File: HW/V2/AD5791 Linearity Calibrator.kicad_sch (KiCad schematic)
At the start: 13 parts, among them J7 Conn_01x32, U1 7533, U2 L78L15, U3 L79L15

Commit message: v2
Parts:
- removed J5, J6: ~, 100mm template footprints:CTB93HD3, symbol Connector_Generic:Conn_01x03
- added C1: 10pF, Resistor_SMD:R_0603_1608Metric, symbol Device:C_Small
- added C1, C3, C4: 10uF, Resistor_SMD:R_0603_1608Metric, symbol Device:C_Small
- added C10, C11, C12, C13, C14, C4, C9: 100nF, Capacitor_SMD:C_0603_1608Metric, symbol Device:C_Small
- added D1, D4: 5819, Resistor_SMD:R_0603_1608Metric_Pad0.98x0.95mm_HandSolder, symbol Device:D_Small
- added H1, H2: MountingHole_Pad, MountingHole:MountingHole_3.2mm_M3_Pad_Via, symbol Mechanical:MountingHole_Pad
- added R1, R2, R3, R4, R5, R6, R7: 10R, Resistor_SMD:R_0603_1608Metric, symbol Device:R
- added SW1: RST, Button_Switch_SMD:SW_SPST_B3U-1000P, symbol Switch:SW_SPST
- added U2: AD5791BRUZ, AD5791BRUZ:SOP65P640X120-20N, symbol AD5791BRUZ:AD5791BRUZ
- added U4: LT1021, Package_DIP:DIP-8_W7.62mm, symbol Reference_Voltage:LT1019xN8
- added U6: +BUFF, Package_SO:SOIC-8_3.9x4.9mm_P1.27mm, symbol Better Op-Amp:Better_Op-Amp
- added U7: -BUFF, Package_SO:SOIC-8_3.9x4.9mm_P1.27mm, symbol Better Op-Amp:Better_Op-Amp
- added U8: Pico, MCU_RaspberryPi_and_Boards:RPi_Pico_SMD_TH, symbol MCU_RaspberryPi_and_Boards:Pico
- added U9: OBUFF, Package_SO:SOIC-8_3.9x4.9mm_P1.27mm, symbol Better Op-Amp:Better_Op-Amp
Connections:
- net GND: now also J1.2 (Pin_2), C1.2, C10.1, C11.1, C12.1, C13.1, C14.1, C3.2, C4.1, C4.2, C9.1, H1.1, H2.1, SW1.1 (A), U2.15 (DGND), U4.4 (GND), U7.3 (+), U8.13 (GND), U8.18 (GND), U8.23 (GND), U8.28 (GND), U8.3 (GND), U8.33 (AGND), U8.37 (3V3_EN), U8.38 (GND), U8.42 (GND), U8.8 (GND)
- net +3.3V: now reaches C1.1, U1.3 (VOUT)
- net +3.3V: now also C3.1, D4.2 (A), U2.10 (IOVCC), U2.9 (VCC), U8.36 (3V3)
- net at U3.2 (VI): now also J1.1 (Pin_1)
- net -15V: now reaches C3.2, U3.3 (VO)
- net -15V: now also C4.1, R5.1, R6.1, R7.1, U2.18 (VSS)
- net +15V: now reaches C2.1, U1.2 (VIN), U2.1 (OUT)
- net +15V: now also C1.1, D4.1 (K), R1.1, R2.1, R3.1, R4.1, U2.5 (VDD)
- net at U2.3 (IN): now also J1.3 (Pin_3)
- new net: C9.2, R2.2, U6.7 (V+)
- new net: C13.2, R6.2, U7.4 (V-)
- new net: SW1.2 (B), U8.30 (RUN)
- new net: C10.2, R3.2, U7.7 (V+)
- new net: C14.2, R7.2, U9.4 (V-)
- new net: C11.2, R4.2, U9.7 (V+)
- new net: C4.2, R1.2, U4.2 (IN)
- new net: C1.1, U2.20 (RFB), U9.6
- new net: C1.2, U2.1 (INV), U9.2 (-)
- new net: C12.2, R5.2, U6.4 (V-)
- new net: D1.2 (A), U8.39 (VSYS)
- new net: U2.2 (VOUT), U9.3 (+)
- new net 10VREF: U4.6 (OUT), U6.3 (+)
- new net 3V3IN: D1.1 (K)
- new net ALERT: U8.21 (GPIO16)
- new net GNDA: U2.19 (AGND)
- new net SCLK: U2.13 (SCLK), U8.7 (GPIO5)
- new net SDIN: U2.12 (SDIN), U8.6 (GPIO4)
- new net SDO: U2.11 (SDO), U8.5 (GPIO3)
- new net UART_RX: U8.2 (GPIO1)
- new net UART_TX: U8.1 (GPIO0)
- new net VREFNF: U2.16 (VREFNF), U7.6
- new net VREFNS: U2.17 (VREFNS), U7.2 (-)
- new net VREFPF: U2.4 (VREFPF), U6.6
- new net VREFPS: U2.3 (VREFPS), U6.2 (-)
- new net ~{CLR}: U2.7 (~{CLR}), U8.11 (GPIO8)
- new net ~{LDAC}: U2.8 (~{LDAC}), U8.12 (GPIO9)
- new net ~{RESET}: U2.6 (~{RESET}), U8.10 (GPIO7)
- new net ~{SYNC}: U2.14 (~{SYNC}), U8.9 (GPIO6)
- no-connect marks 0 -> 9
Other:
- note added: "On-board 3V3 reg deactivated"
- moved on the sheet: J1, J2, J3, J4, J7

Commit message: finalized schematics for v2
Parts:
- removed C1: 10pF, Resistor_SMD:R_0603_1608Metric, symbol Device:C_Small
- removed C4: 100nF, Capacitor_SMD:C_0603_1608Metric, symbol Device:C_Small
- removed D1: 5819, Resistor_SMD:R_0603_1608Metric_Pad0.98x0.95mm_HandSolder, symbol Device:D_Small
- removed R1: 10R, Resistor_SMD:R_0603_1608Metric, symbol Device:R
- removed U4: LT1021, Package_DIP:DIP-8_W7.62mm, symbol Reference_Voltage:LT1019xN8
- removed U6: +BUFF, Package_SO:SOIC-8_3.9x4.9mm_P1.27mm, symbol Better Op-Amp:Better_Op-Amp
- removed U7: -BUFF, Package_SO:SOIC-8_3.9x4.9mm_P1.27mm, symbol Better Op-Amp:Better_Op-Amp
- removed U9: OBUFF, Package_SO:SOIC-8_3.9x4.9mm_P1.27mm, symbol Better Op-Amp:Better_Op-Amp
- added C16, C2: 1uF, Resistor_SMD:R_0603_1608Metric, symbol Device:C_Small
- added D3: 5819, Resistor_SMD:R_0603_1608Metric_Pad0.98x0.95mm_HandSolder, symbol Device:D_Small
- added JP1: DACOUT, Connector_PinHeader_2.54mm:PinHeader_1x02_P2.54mm_Vertical, symbol Jumper:SolderJumper_2_Bridged
- added R2: 1K, Resistor_SMD:R_0603_1608Metric, symbol Device:R
- added R3: 5R1, Resistor_SMD:R_0603_1608Metric, symbol Device:R
- added R4: 100K, Resistor_SMD:R_0603_1608Metric, symbol Device:R
- added RN1: 10K, Package_SO:SOIC-16_3.9x9.9mm_P1.27mm, symbol Device:R_Pack08_Split
- added U3: ADR1399, Package_TO_SOT_THT:Analog_TO-46-4_ThermalShield, symbol Reference_Voltage:LM399
- added U6: REFSCALE, Package_SO:SOIC-8_3.9x4.9mm_P1.27mm, symbol Device:Opamp_Dual
- added U7: REFBUF, Package_SO:SOIC-8_3.9x4.9mm_P1.27mm, symbol Device:Opamp_Dual
- added U9: OUTBUF, Package_SO:SOIC-8_3.9x4.9mm_P1.27mm, symbol Device:Opamp_Dual
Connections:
- net +15V: now also C16.1, R4.1, U3.3
- net -15V: now also C16.2, U3.4
- net GND: now also U6.5 (+)
- net GNDA: now also C2.2, U3.2, U9.5 (+)
- net VREFNF: now also U7.7
- net VREFNS: now also U7.6 (-)
- net VREFPF: now also D3.2 (A), U7.1
- net VREFPS: now also U7.2 (-)
- net at C9.2, R2.2: now also U7.8 (V+)
- net at C13.2, R6.2: now also U9.4 (V-)
- net at C10.2, R3.2: now also U9.8 (V+)
- net at C14.2, R7.2: now also U6.4 (V-)
- net at C11.2, R4.2: now also U6.8 (V+)
- net at C12.2, R5.2: now also U7.4 (V-)
- net at U2.2 (VOUT): now also JP1.1 (A)
- new net: D3.1 (K), R2.2
- new net: RN1.11 (R6.2), RN1.3 (R3.1)
- new net: RN1.6 (R6.1), RN1.9 (R8.2)
- new net: U9.6 (-), U9.7
- new net: U9.1, U9.2 (-)
- new net: JP1.2 (B), U9.3 (+)
- new net: C2.1, R3.2
- new net: RN1.12 (R5.2), RN1.4 (R4.1), U6.2 (-)
- new net: RN1.10 (R7.2), RN1.5 (R5.1)
- new net: RN1.7 (R7.1), RN1.8 (R8.1), U6.6 (-)
- new net +10.5V: RN1.13 (R4.2), U6.1, U7.3 (+)
- new net -10.5V: RN1.14 (R3.2), U6.7, U7.5 (+)
- new net 7VREF: R2.1, R3.1, R4.2, U3.1, U6.3 (+)
- no-connect marks 9 -> 2
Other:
- note added: "Select for 3mA Iz"
- moved on the sheet: C1, C2, C3, C4, D4, J1, U1, U2, U3

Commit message: updated v2 PCB files
finalized layout?
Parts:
- removed J2, J3: ~, 100mm template footprints:CTB93HD3, symbol Connector_Generic:Conn_01x03
- removed J7: Conn_01x32, 100mm template footprints:SIL32, symbol Connector_Generic:Conn_01x32
- removed U1: 7533, Package_TO_SOT_SMD:SOT-89-3, symbol Regulator_Linear:HT75xx-1-SOT89
- removed U2: L78L15, Package_TO_SOT_SMD:SOT-89-3, symbol Regulator_Linear:L78L15_SOT89
- removed U3: L79L15, Package_TO_SOT_SMD:SOT-89-3, symbol Regulator_Linear:L79L15_SOT89
- added JP2: DACOUT, Connector_PinHeader_1.27mm:PinHeader_1x02_P1.27mm_Vertical, symbol Jumper:SolderJumper_2_Bridged
- added R10, R12, R14: 220R, Resistor_SMD:R_0603_1608Metric, symbol Device:R
- added R11, R13: 2K4, Resistor_SMD:R_0603_1608Metric, symbol Device:R
- added R15: 390R, Resistor_SMD:R_0603_1608Metric, symbol Device:R
- added U1, U3: LM317, Package_TO_SOT_SMD:TO-252-2, symbol Regulator_Linear:LM317_TO-252
- added U2: LM337, Package_TO_SOT_SMD:TO-252-2, symbol Regulator_Linear:LM337_TO252
- C1, C16, C2, C3, C4: footprint Resistor_SMD:R_0603_1608Metric -> Capacitor_SMD:C_0603_1608Metric
- H1, H2: footprint MountingHole:MountingHole_3.2mm_M3_Pad_Via -> MountingHole:MountingHole_3.2mm_M3_DIN965_Pad
- JP1: footprint Connector_PinHeader_2.54mm:PinHeader_1x02_P2.54mm_Vertical -> Connector_PinHeader_1.27mm:PinHeader_1x02_P1.27mm_Vertical
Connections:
- net +10.5V: now also D3.2 (A), RN1.15 (R2.2), U6.7; no longer RN1.13 (R4.2), U6.1
- net +15V: now also R10.1, U1.2 (VO), U3.3 (VI)
- net +3.3V: now also R14.1, U3.2 (VO)
- net -10.5V: now also RN1.7 (R7.1), U6.1; no longer RN1.14 (R3.2), U6.7
- net -15V: now also R12.2, U2.3 (VO)
- net 7VREF: now also U6.5 (+); no longer U6.3 (+)
- net GND: now also JP2.2 (B), R11.2, R13.1, R15.2; no longer U6.5 (+)
- net GNDA: now also J4.2 (Pin_2), U6.3 (+), JP2.1 (A)
- net VREFPF: no longer D3.2 (A)
- net at RN1.11 (R6.2): now also RN1.12 (R5.2); no longer RN1.3 (R3.1)
- net at RN1.6 (R6.1): now also RN1.10 (R7.2); no longer RN1.9 (R8.2)
- net at J1.1 (Pin_1): now also U2.2 (VI)
- net at U9.6 (-), U9.7: now also J4.3 (Pin_3)
- net at U9.1, U9.2 (-): now also J4.1 (Pin_1)
- net BUFIN: now reaches JP1.2 (B), U9.3 (+)
- net BUFIN: now also JP1.1 (A), U2.2 (VOUT)
- net at J1.3 (Pin_3): now also U1.3 (VI)
- net at RN1.4 (R4.1), U6.2 (-): now also RN1.5 (R5.1); no longer RN1.12 (R5.2)
- net at RN1.2 (R2.1): now also RN1.3 (R3.1), U6.6 (-)
- new net: R14.2, R15.1, U3.1 (ADJ)
- new net: R12.1, R13.2, U2.1 (ADJ)
- new net: R10.2, R11.1, U1.1 (ADJ)
- new net: RN1.13 (R4.2), RN1.14 (R3.2)
- now unconnected: RN1.8 (R8.1)
- no-connect marks 2 -> 6
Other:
- note added: "3mA Iz"
- note removed: "Select for 3mA Iz"
- moved on the sheet: C1, C2, C3, J1, J4, JP1, RN1A, RN1B, RN1C, RN1D, RN1E, RN1F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

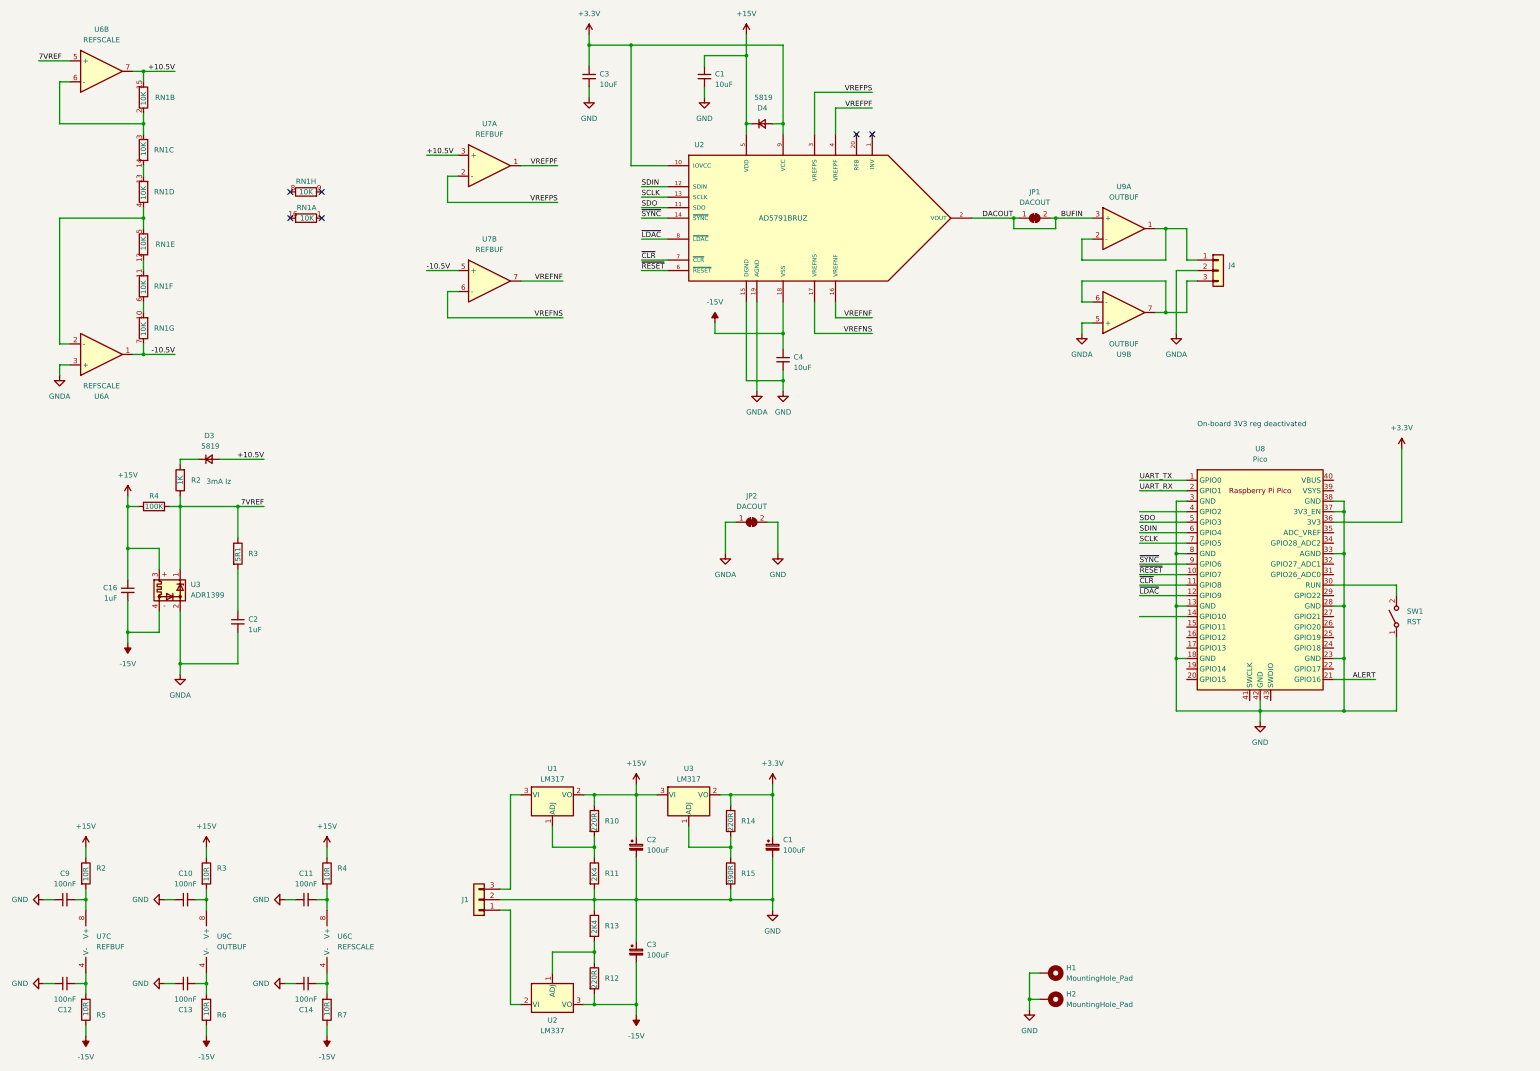
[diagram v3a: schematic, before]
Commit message: updated v2 layout
added isolator, artwork, finalized placement
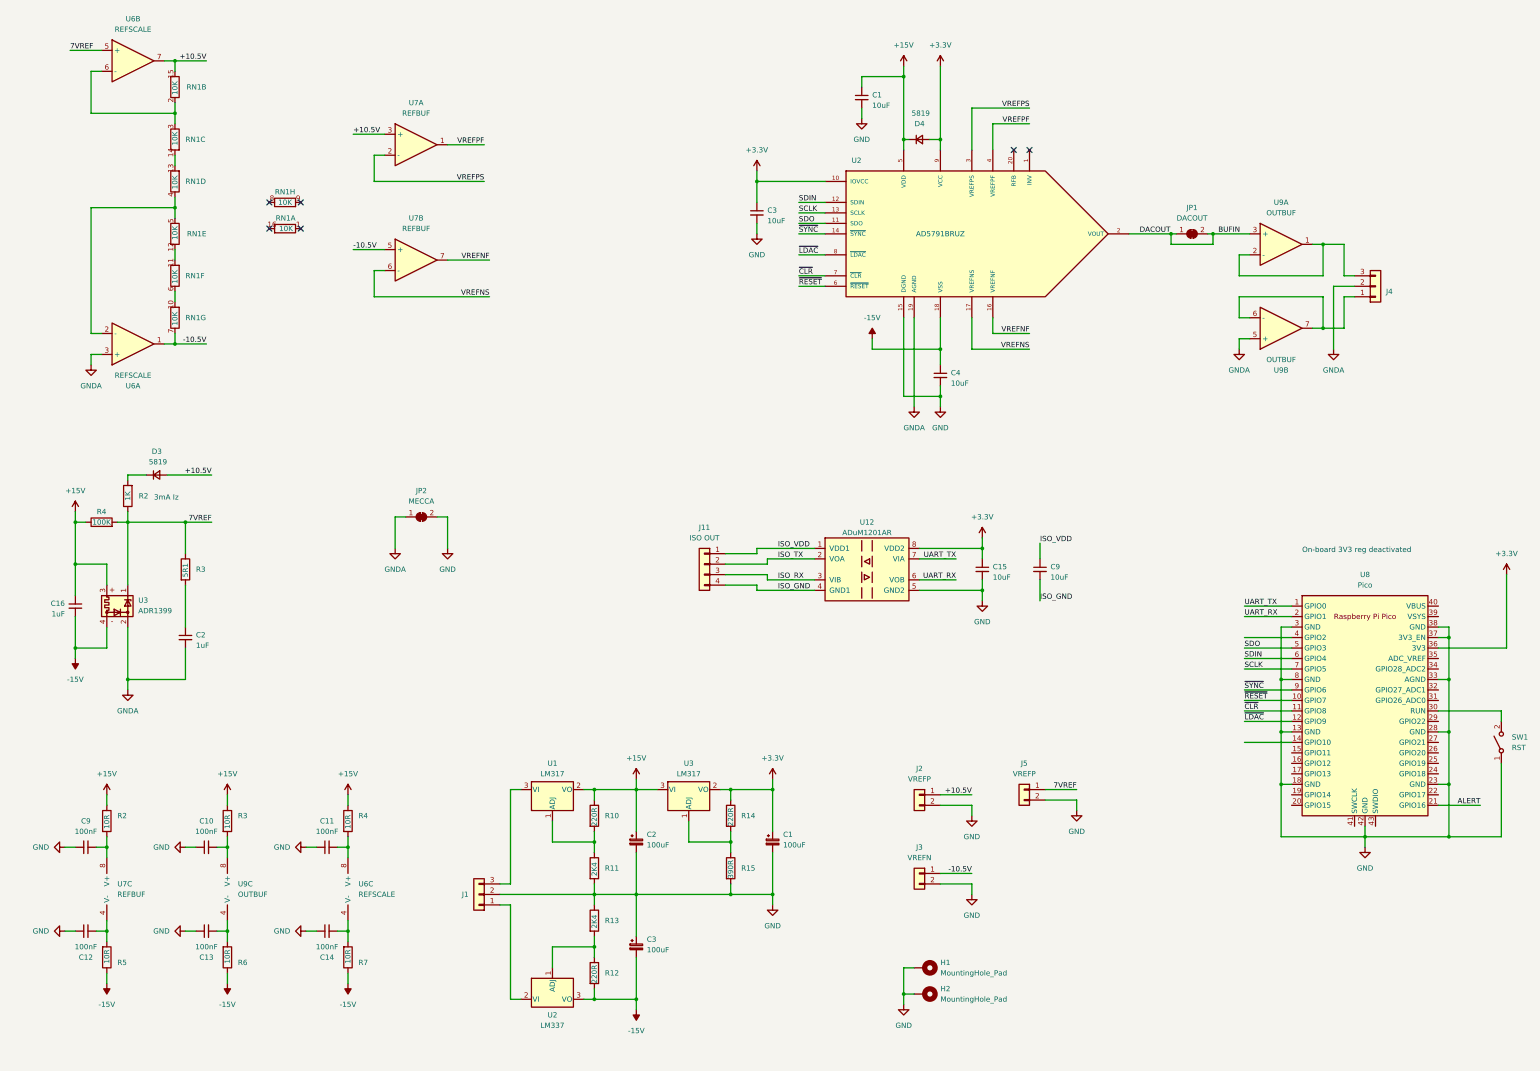
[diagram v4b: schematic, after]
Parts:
- added C15, C9: 10uF, Resistor_SMD:R_0603_1608Metric, symbol Device:C_Small
- added J11: ISO OUT, Connector_PinHeader_2.54mm:PinHeader_1x04_P2.54mm_Vertical, symbol Connector_Generic:Conn_01x04
- added J2, J5: VREFP, Connector_PinHeader_1.27mm:PinHeader_1x02_P1.27mm_Vertical, symbol Connector_Generic:Conn_01x02
- added J3: VREFN, Connector_PinHeader_1.27mm:PinHeader_1x02_P1.27mm_Vertical, symbol Connector_Generic:Conn_01x02
- added U12: ADuM1201AR, Package_SO:SOIC-8_3.9x4.9mm_P1.27mm, symbol Isolator:ADuM1201AR
- JP2: value DACOUT -> MECCA
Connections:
- net +10.5V: now also J2.1 (Pin_1)
- net +3.3V: now also C15.1, U12.8 (VDD2)
- net -10.5V: now also J3.1 (Pin_1)
- net 7VREF: now also J5.1 (Pin_1)
- net GND: now also C15.2, J2.2 (Pin_2), J3.2 (Pin_2), J5.2 (Pin_2), U12.5 (GND2)
- net UART_RX: now also U12.6 (VOB)
- net UART_TX: now also U12.7 (VIA)
- net at U9.6 (-), U9.7: now also J4.1 (Pin_1); no longer J4.3 (Pin_3)
- net at U9.1, U9.2 (-): now also J4.3 (Pin_3); no longer J4.1 (Pin_1)
- new net ISO_GND: C9.2, J11.4 (Pin_4), U12.4 (GND1)
- new net ISO_RX: J11.3 (Pin_3), U12.3 (VIB)
- new net ISO_TX: J11.2 (Pin_2), U12.2 (VOA)
- new net ISO_VDD: C9.1, J11.1 (Pin_1), U12.1 (VDD1)
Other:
- moved on the sheet: C1, C10, C11, C12, C13, C14, C16, C2, C3, C4, C9, D3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

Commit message: updated files
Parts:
- added J11: PWR, Connector_PinHeader_2.54mm:PinHeader_1x04_P2.54mm_Vertical, symbol Connector_Generic:Conn_01x04
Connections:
- net ISO_GND: now also J11.1 (Pin_1); no longer J11.4 (Pin_4)
- net ISO_RX: now also J11.2 (Pin_2); no longer J11.3 (Pin_3)
- net ISO_TX: now also J11.3 (Pin_3); no longer J11.2 (Pin_2)
- net ISO_VDD: now also J11.4 (Pin_4); no longer J11.1 (Pin_1)
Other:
- moved on the sheet: J11
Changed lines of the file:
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@@
     )
   )
-  (symbol (lib_id "Connector_Generic:Conn_01x04") (at 191.77 157.48 0) (mirror y) (unit 1)
-    (in_bom yes) (on_board yes) (dnp no)
-    (property "Reference" "J11" (at 191.77 148.59 0)
-      (effects (font (size 1.27 1.27)))
-    )
-    (property "Value" "ISO OUT" (at 191.77 151.13 0)
-      (effects (font (size 1.27 1.27)))
-    )
-    (property "Footprint" "Connector_PinHeader_2.54mm:PinHeader_1x04_P2.54mm_Vertical" (at 191.77 157.48 0)
-      (effects (font (size 1.27 1.27)) hide)
-    )
-    (property "Datasheet" "~" (at 191.77 157.48 0)
+  (symbol (lib_id "Connector_Generic:Conn_01x04") (at 191.77 160.02 180) (unit 1)
+    (in_bom yes) (on_board yes) (dnp no)
+    (property "Reference" "J11" (at 191.77 168.91 0)
+      (effects (font (size 1.27 1.27)))
+    )
+    (property "Value" "ISO OUT" (at 191.77 166.37 0)
+      (effects (font (size 1.27 1.27)))
+    )
+    (property "Footprint" "Connector_PinHeader_2.54mm:PinHeader_1x04_P2.54mm_Vertical" (at 191.77 160.02 0)
+      (effects (font (size 1.27 1.27)) hide)
+    )
+    (property "Datasheet" "~" (at 191.77 160.02 0)
       (effects (font (size 1.27 1.27)) hide)
     )
@@
         )
       )
+    )
+  )
+  (symbol (lib_id "Connector_Generic:Conn_01x04") (at 267.97 236.22 0) (mirror y) (unit 1)
+    (in_bom yes) (on_board yes) (dnp no)
+    (property "Reference" "J11" (at 267.97 227.33 0)
+      (effects (font (size 1.27 1.27)))
+    )
+    (property "Value" "PWR" (at 267.97 229.87 0)
+      (effects (font (size 1.27 1.27)))
+    )
+    (property "Footprint" "Connector_PinHeader_2.54mm:PinHeader_1x04_P2.54mm_Vertical" (at 267.97 236.22 0)
+      (effects (font (size 1.27 1.27)) hide)
+    )
+    (property "Datasheet" "~" (at 267.97 236.22 0)
+      (effects (font (size 1.27 1.27)) hide)
+    )
+    (pin "1")
+    (pin "2")
+    (pin "3")
+    (pin "4")
+    (instances
+      (project "AD5791 Linearity Calibrator"
+        (path "/545249ea-2c8e-4b30-8f2b-5f4518163292"
+          (reference "J11") (unit 1)
+        )
+      )
+      (project "AD5791 Linearity Calibrator"
+        (path "/e4c8fe5c-4d6c-45a9-911b-05eafd37681e"
+          (reference "J7") (unit 1)
+        )
+      )
